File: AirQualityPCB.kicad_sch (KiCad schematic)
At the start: 32 parts, among them J1 TestPoint 5V, J10 ProgPoint GND, J2 USB_C_Receptacle_USB2.0_16P, J3 TestPoint GND, J4 TestPoint 3.3V, J6 ProgPoint 5V, J7 ProgPoint P9 GND, J8 ProgPointPoint D_P, J9 ProgPoint D_N, U1 Regulator, U2 USBLC6-2SC6, U3 PTS526 SK15 SMTR2 LFS, U4 ESP32-C3-WROOM-02U

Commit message: Finished schematic
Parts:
- removed D2: RED LED, LED_SMD:LED_0603_1608Metric, symbol Device:LED
- removed R6: 75, Resistor_SMD:R_1206_3216Metric, symbol Device:R
- removed U4: ESP32-C3-WROOM-02U, RF_Module:ESP32-C3-WROOM-02U, symbol RF_Module:ESP32-C3-WROOM-02U
- added J10: SMA-J-P-H-ST-EM1, Connector_Coaxial:SMA_Samtec_SMA-J-P-H-ST-EM1_EdgeMount, symbol Connector:Conn_Coaxial
- added U13: ESP32-C3-WROOM-02, RF_Module:ESP32-C3-WROOM-02, symbol RF_Module:ESP32-C3-WROOM-02
- added U4: RFM95WCW, RF_Module:HOPERF_RFM9XW_SMD, symbol Sensors:RFM95WCW
- R4: value 75 -> 1k; Manufacturer Part Number CRCW120675R0FKEA -> RC1206FR-071KL
- renumbered C6 to C3, J2 to J1, J1 to J2, J6 to J5, J7 to J6, J8 to J7, J9 to J8, J10 to J9
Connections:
- net +3.3V: now also U13.1 (3V3), U4.5 (3.3V)
- net D+: now also U13.14 (IO19)
- net D-: now also U13.13 (IO18)
- net GND: now also J10.2 (Ext), U13.19 (GND), U13.9 (GND), U4.16 (GND), U4.2 (GND), U4.9 (GND)
- net SCL: now also U13.4 (IO5)
- net SDA: now also U13.3 (IO4)
- net LED: now reaches R10.2
- net LED: now also R4.2, U13.7 (IO8)
- net at R9.2: now also U13.16 (IO2)
- net at C3.2, R8.2: now also U13.2 (EN)
- net at R7.2, U3.1: now also U13.8 (IO9)
- new net: J10.1 (In), U4.1 (ANT)
- new net CS: U13.10 (IO10), U4.13 (NSS)
- new net DIO0: U13.12 (IO21/TXD), U4.6 (DIO0)
- new net DIO1: U13.11 (IO20/RXD), U4.7 (DIO1)
- new net DIO2: U4.8 (DIO2)
- new net MISO: U13.6 (IO7), U4.10 (MISO)
- new net MOSI: U13.5 (IO6), U4.11 (MOSI)
- new net SCK: U13.15 (IO3), U4.12 (SCK)
- new net Sensor_RX: U13.18 (IO0)
- new net Sensor_TX: U13.17 (IO1)
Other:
- sheet Sensors ports: added SCL, SDA, Sensor_RX, Sensor_TX; removed none
- note added: "Use UART1 for these"
- moved on the sheet: D1, R10, R4

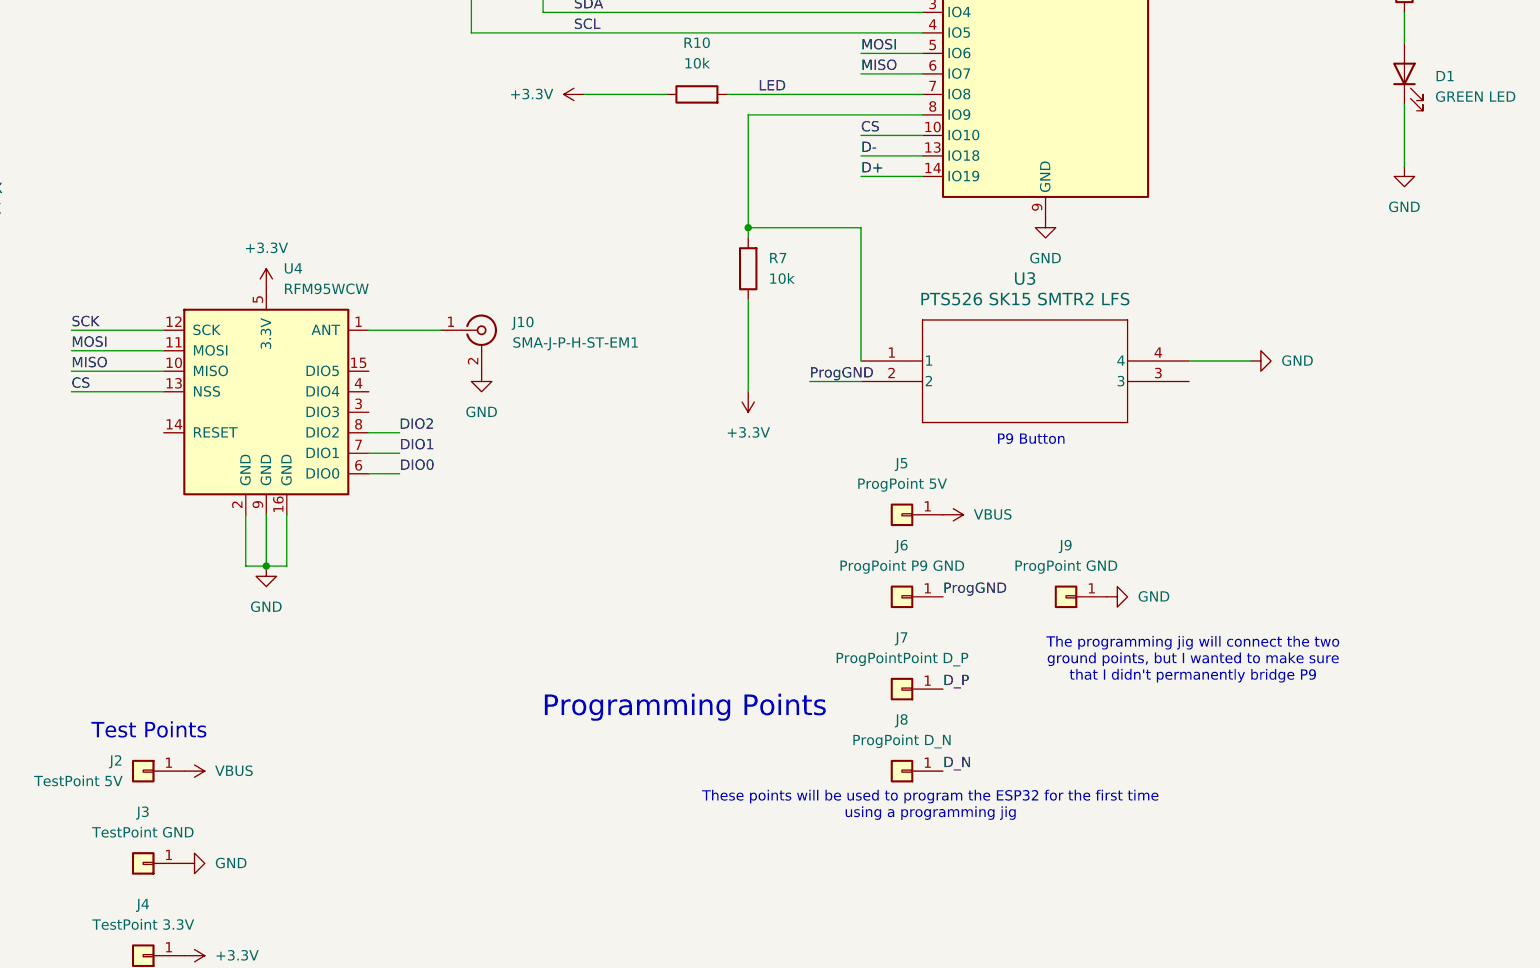
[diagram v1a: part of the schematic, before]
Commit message: Finished first footprint (no routing)
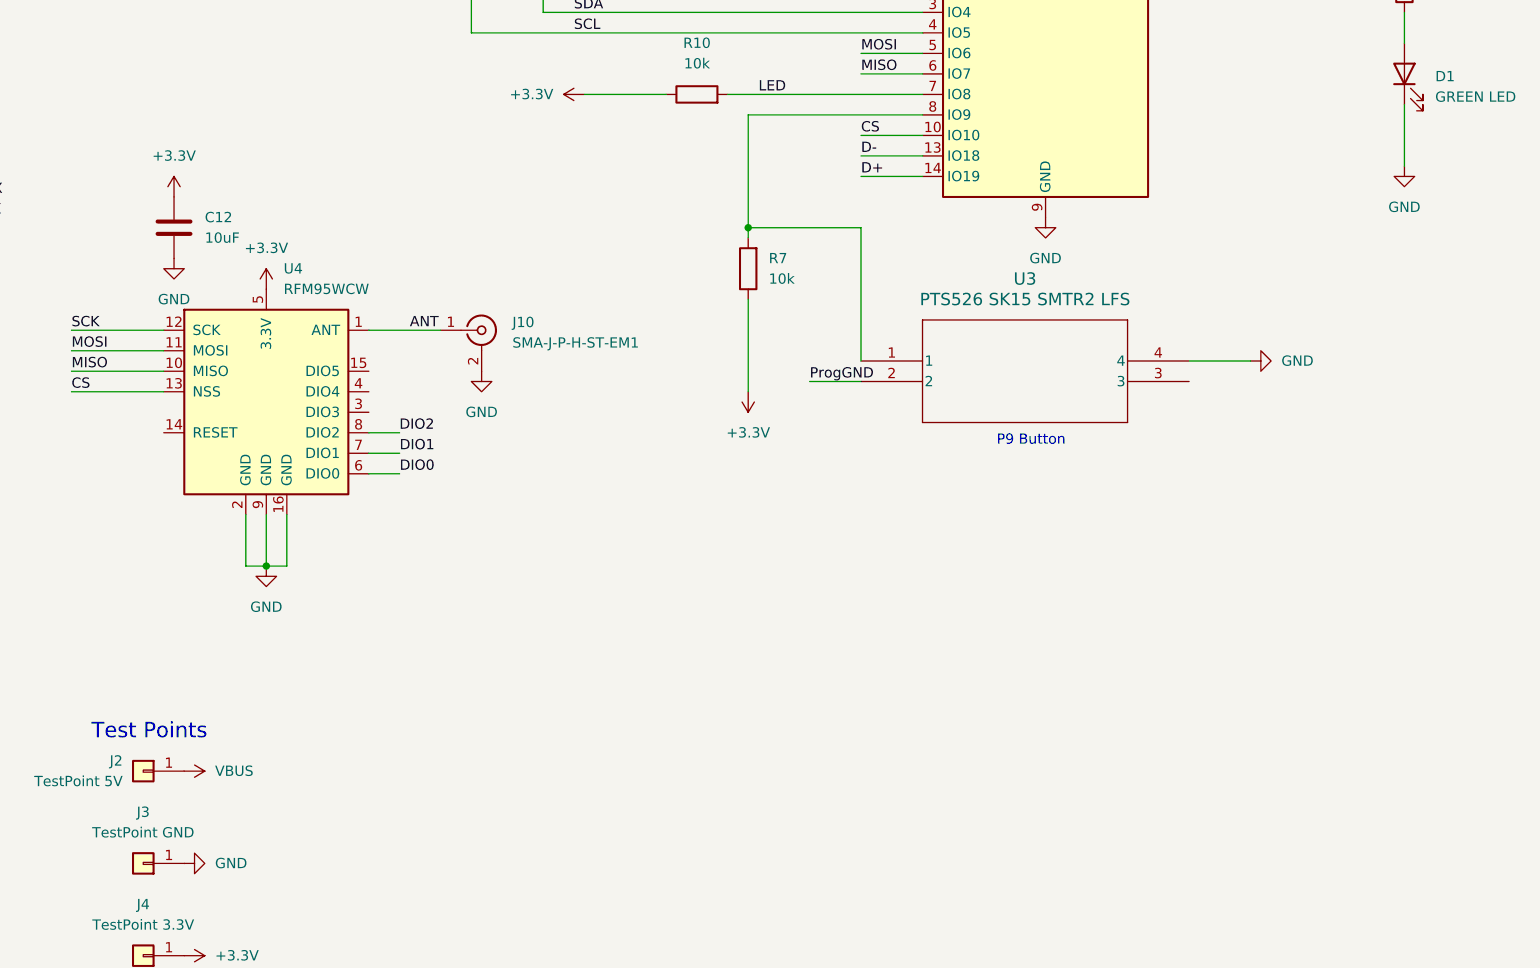
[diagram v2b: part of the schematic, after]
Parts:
- removed J5: ProgPoint 5V, TestPoint:TestPoint_Pad_D1.0mm, symbol Connector_Generic:Conn_01x01
- removed J6: ProgPoint P9 GND, TestPoint:TestPoint_Pad_D1.0mm, symbol Connector_Generic:Conn_01x01
- removed J7: ProgPointPoint D_P, TestPoint:TestPoint_Pad_D1.0mm, symbol Connector_Generic:Conn_01x01
- removed J8: ProgPoint D_N, TestPoint:TestPoint_Pad_D1.0mm, symbol Connector_Generic:Conn_01x01
- removed J9: ProgPoint GND, TestPoint:TestPoint_Pad_D1.0mm, symbol Connector_Generic:Conn_01x01
- added C12: 10uF, Capacitor_SMD:C_1206_3216Metric, symbol Device:C
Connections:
- net +3.3V: now also C12.2
- net GND: now also C12.1
- net ANT: now reaches J10.1 (In), U4.1 (ANT)
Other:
- note removed: "Programming Points"
- note removed: "The programming jig will connect the two ground points, but I wanted to make sure that I didn't permanently bridge P9"
- note removed: "These points will be used to program the ESP32 for the first time using a programming jig"

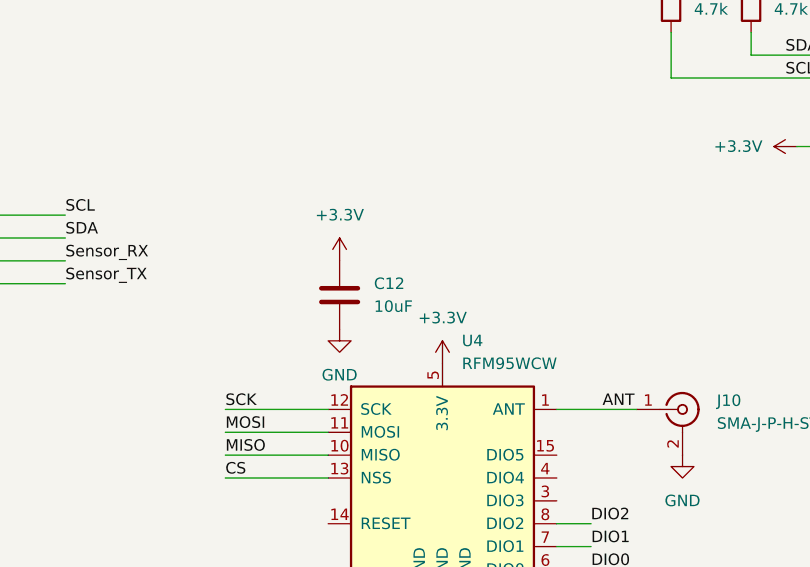
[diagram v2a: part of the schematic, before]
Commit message: Removed components pre quilter routing
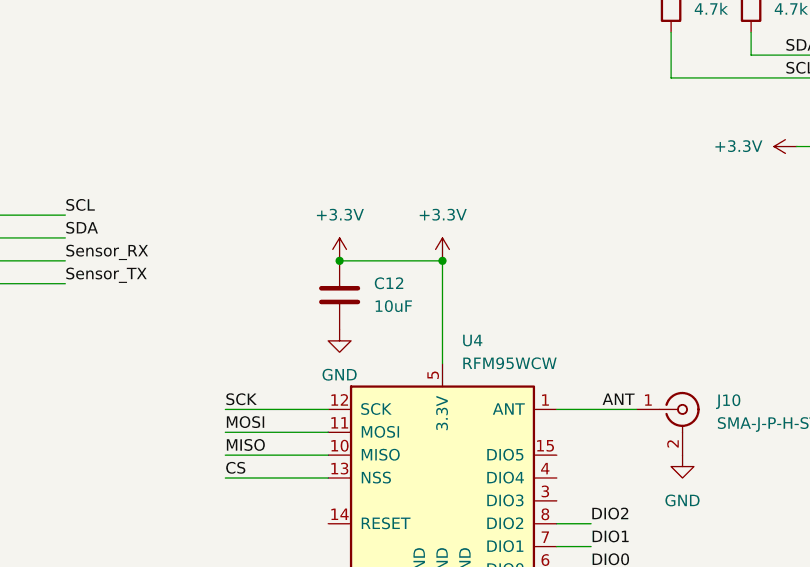
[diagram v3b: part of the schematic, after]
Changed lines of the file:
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@@
 	)
 	(junction
+		(at 137.16 88.9)
+		(diameter 0)
+		(color 0 0 0 0)
+	)
+	(junction
 		(at 27.94 34.29)
 		(diameter 0)
@@
 	)
 	(junction
+		(at 125.73 88.9)
+		(diameter 0)
+		(color 0 0 0 0)
+	)
+	(junction
 		(at 57.15 153.67)
 		(diameter 0)
@@
 	(wire
 		(pts
+			(xy 137.16 88.9) (xy 137.16 100.33)
+		)
+		(stroke
+			(width 0)
+			(type default)
+		)
+	)
+	(wire
+		(pts
 			(xy 93.98 39.37) (xy 97.79 39.37)
 		)
@@
 	(wire
 		(pts
+			(xy 125.73 88.9) (xy 137.16 88.9)
+		)
+		(stroke
+			(width 0)
+			(type default)
+		)
+	)
+	(wire
+		(pts
 			(xy 27.94 45.72) (xy 27.94 50.8)
 		)
@@
 	(symbol
 		(lib_id "power:+3.3V")
-		(at 137.16 100.33 0)
+		(at 137.16 88.9 0)
 		(unit 1)
 		(exclude_from_sim no)
@@
 		(fields_autoplaced yes)
 		(property "Reference" "#PWR051"
-			(at 137.16 104.14 0)
+			(at 137.16 92.71 0)
 			(effects
 				(font
@@
 		)
 		(property "Value" "+3.3V"
-			(at 137.16 95.25 0)
+			(at 137.16 83.82 0)
 			(effects
 				(font
@@
 		)
 		(property "Footprint" ""
-			(at 137.16 100.33 0)
+			(at 137.16 88.9 0)
 			(effects
 				(font
@@
 		)
 		(property "Datasheet" ""
-			(at 137.16 100.33 0)
+			(at 137.16 88.9 0)
 			(effects
 				(font
@@
 		)
 		(property "Description" "Power symbol creates a global label with name \"+3.3V\""
-			(at 137.16 100.33 0)
+			(at 137.16 88.9 0)
 			(effects
 				(font

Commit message: v1.0 done
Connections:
- net GND: now also J1.S1 (SHIELD)
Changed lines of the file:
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@@
 	(title_block
 		(title "AirQualityPCB")
-		(date "2026-03-22")
+		(date "2026-03-25")
 		(rev "1.0")
 		(company "Cornell University")
@@
 					(unit 1)
 				)
+			)
+		)
+	)
+	(symbol
+		(lib_id "power:GND")
+		(at 30.48 172.72 0)
+		(unit 1)
+		(exclude_from_sim no)
+		(in_bom yes)
+		(on_board yes)
+		(dnp no)
+		(fields_autoplaced yes)
+		(property "Reference" "#PWR020"
+			(at 30.48 179.07 0)
+			(effects
+				(font
+					(size 1.27 1.27)
+				)
+				(hide yes)
+			)
+		)
+		(property "Value" "GND"
+			(at 30.48 177.8 0)
+			(effects
+				(font
+					(size 1.27 1.27)
+				)
+			)
+		)
+		(property "Footprint" ""
+			(at 30.48 172.72 0)
+			(effects
+				(font
+					(size 1.27 1.27)
+				)
+				(hide yes)
+			)
+		)
+		(property "Datasheet" ""
+			(at 30.48 172.72 0)
+			(effects
+				(font
+					(size 1.27 1.27)
+				)
+				(hide yes)
+			)
+		)
+		(property "Description" "Power symbol creates a global label with name \"GND\" , ground"
+			(at 30.48 172.72 0)
+			(effects
+				(font
+					(size 1.27 1.27)
+				)
+				(hide yes)
+			)
+		)
+		(pin "1"
+		)
+		(instances
+			(project "AirQualityPCB"
+				(path "/91f71406-0d85-449c-a1a7-616be8373eb5"
+					(reference "#PWR020")
+					(unit 1)
+				)
